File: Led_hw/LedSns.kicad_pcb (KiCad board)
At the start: 2 copper layers, 22 x 11.5 mm, 6 parts

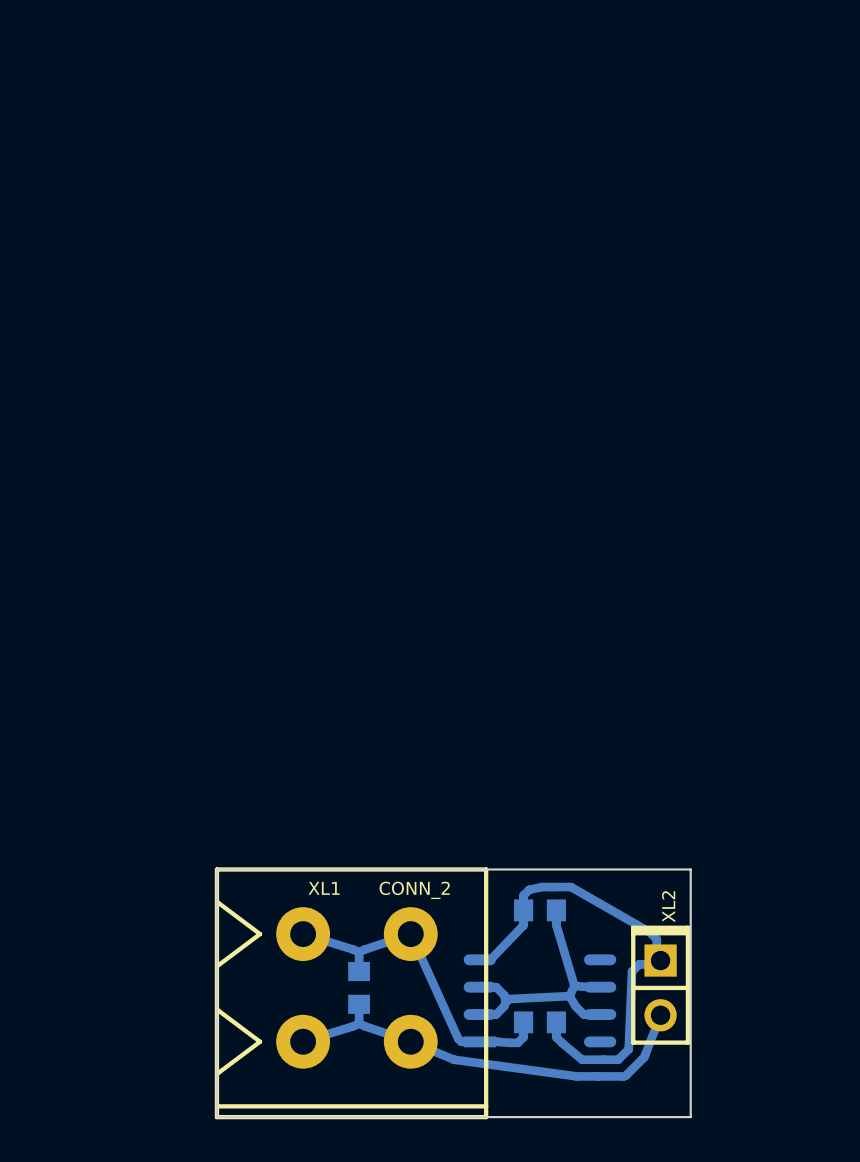
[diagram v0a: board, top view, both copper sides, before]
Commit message: + LedSNS completed PCBs sent to production
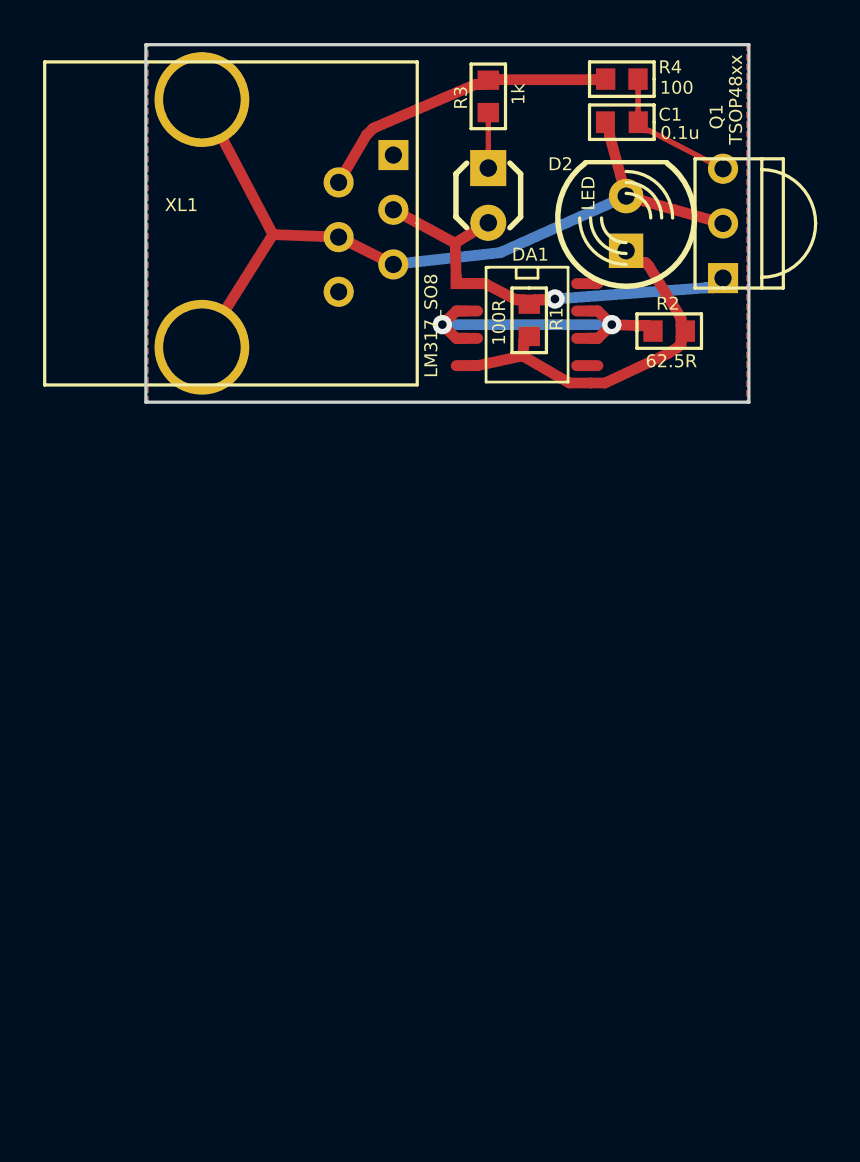
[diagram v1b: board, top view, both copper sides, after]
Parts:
- removed XL2: CONN_2, CONN_PLS-2
- added D1: LED, LEDs:Through-Hole-3mm, F.Cu at (171.6, 91.2)
- added D2: LED, LEDs:Through-Hole-5mm, F.Cu at (178.0, 92.5)
- added Q1: TSOP48xx, Sensors:TSOP48xx, F.Cu at (182.5, 92.5)
- added R3: 1k, Resistors:RES_0603, F.Cu at (171.6, 86.6)
- added R4: 100, Resistors:RES_0603, F.Cu at (177.8, 85.8)
- C1: footprint CAP_0603 -> Capacitors:CAP_0603; moved to F.Cu
- DA1: footprint SO8E -> SO_DIL_TSSOP:SO8; moved to F.Cu
- R1, R2: footprint RES_0603 -> Resistors:RES_0603; moved to F.Cu
- XL1: value CONN_2 -> RJ11; footprint SPRING_TERM_XY124V_A_2 -> Connectors:RJ11_TJ6_6P6C
- moved C1 42.0 mm to (177.8, 87.8), turned to 180 degrees
- moved XL1 38.3 mm to (151.0, 92.5), turned to 0 degrees
- moved R1 32.6 mm to (173.5, 97.0), turned to 270 degrees
- moved DA1 31.4 mm to (173.4, 97.2), turned to 270 degrees
- moved R2 27.6 mm to (180.0, 97.5), turned to 0 degrees
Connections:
- C1 pad 1: N-000002 -> Net-(C1-Pad1)
- DA1 pad 1: N-000002 -> /LED_SNS
- R1 pad 1: N-000002 -> /LED_SNS
- XL1 pad 1: N-000002 -> (no net)
- XL1 pad 2: GND -> +5V
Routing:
- net /LED_SNS: track 0.00 -> 19.9 mm, vias 0 -> 1
- net GND: track 19.7 -> 38.8 mm
- net N-000002: track 15.4 -> 0.00 mm
- net +5V: track 0.00 -> 14.3 mm
- net Net-(C1-Pad1): track 0.00 -> 6.55 mm
- net Net-(D2-PadA): track 21.9 -> 17.3 mm
- net Net-(D1-PadA): track 0.00 -> 2.58 mm
- net Net-(DA1-Pad2): track 13.3 -> 15.5 mm, vias 0 -> 2
- added copper zone on B.Cu, net GND
- added copper zone on F.Cu, net GND
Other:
- board size 22 x 11.5 mm -> 28 x 16.6 mm
- net class Default: clearance 0.25 -> 0.2; trace_width 0.4 -> 0.25; via_dia 0.889 -> 0.9; via_drill 0.635 -> 0.4
- net class Wide added: clearance 0.2, trace_width 0.5, via_dia 0.9, via_drill 0.4
- rule trace_clearance: 0.25 -> 0.2
- rule trace_min: 0.254 -> 0.2
- rule via_min_drill: 0.508 -> 0.3
- rule via_min_size: 0.889 -> 0.4
